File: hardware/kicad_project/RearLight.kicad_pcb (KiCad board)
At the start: 2 copper layers, 26 x 55.5 mm, 55 parts, among them J1 USB_C_Receptacle_USB2.0_16P, J2 Conn_02x03_Odd_Even, Q1 AO3400A, Q3 AO3400A, SW1 SW_Push, U1 453-00039R, U2 USBLC6-2SC6, U4 DW01A, U5 LIS3DH, U6 OPT3001DNPR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

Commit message: Layout 2nd draft
Todo: increase via size
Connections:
- U1 pad 33: GND -> unconnected-(U1-GND-Pad33)
- U1 pad 47: GND -> unconnected-(U1-GND-Pad47)
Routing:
- net GND: track 61.9 -> 92.6 mm, vias 46 -> 71
- net Net-(LED1-K): track 7.74 -> 0.00 mm
- net +VDD_nRF: track 121.4 -> 128.1 mm, vias 9 -> 10
- net Net-(LED1-A): track 4.80 -> 0.00 mm
- added copper zone on F.Cu, net Net-(LED1-A)
- added copper zone on F.Cu, net Net-(LED1-K)

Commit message: DFM design overhaul
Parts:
- removed H1, H2, H3, H4: M2, MountingHole:MountingHole_2.1mm
- removed LED2: LTRB_RASF.01-6B6C-C3E6-0-0-R18, RearLight:LTRBRASF016B6CC3E600R18
- removed R19: 100, Resistor_SMD:R_0402_1005Metric
- added D1: LED_R, LED_SMD:LED_0603_1608Metric, F.Cu at (150.5, 111.0)
- added D2: LED_Y, LED_SMD:LED_0805_2012Metric, F.Cu at (153.0, 110.8)
- added R16: 49R9, RearLight:R_0402_1005Metric_NO_SILK, F.Cu at (153.0, 113.6)
- C2, C3: footprint Capacitor_SMD:C_0603_1608Metric -> RearLight:C_0603_1608Metric_NO_SILK
- R1, R11, R5: footprint Resistor_SMD:R_0603_1608Metric -> RearLight:R_0603_1608Metric_NO_SILK
- R10, R12, R13, R14, R2, R3, R4, R6, R7, R8: footprint Resistor_SMD:R_0402_1005Metric -> RearLight:R_0402_1005Metric_NO_SILK
- U1: footprint Liard_BL653_ 453-00039_Custom:Laird_BL653 -> RF_Module:Laird_BL653
- moved R10 4.91 mm to (150.5, 113.6), turned to 90 degrees
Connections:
- U1 pad 22: RGB_B -> unconnected-(U1-SIO_14-Pad22)
- U1 pad 27: RGB_R -> RGB_Y
- U1 pad 28: RGB_G -> RGB_R
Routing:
- net RGB_B: track 14.3 -> 0.00 mm, vias 2 -> 0
- net RGB_G: track 10.8 -> 0.00 mm, vias 2 -> 0
- net RGB_Y: track 0.00 -> 9.81 mm
- net +VDD_nRF: track 128.1 -> 119.5 mm
- net Net-(LED2-A_RED): track 5.90 -> 0.00 mm
- net Net-(D1-A): track 6.60 -> 1.30 mm
- net Net-(D2-A): track 0.00 -> 1.34 mm
- net GND: track 92.6 -> 93.5 mm, vias 71 -> 72
- net RGB_R: track 9.46 -> 9.87 mm, vias 0 -> 2

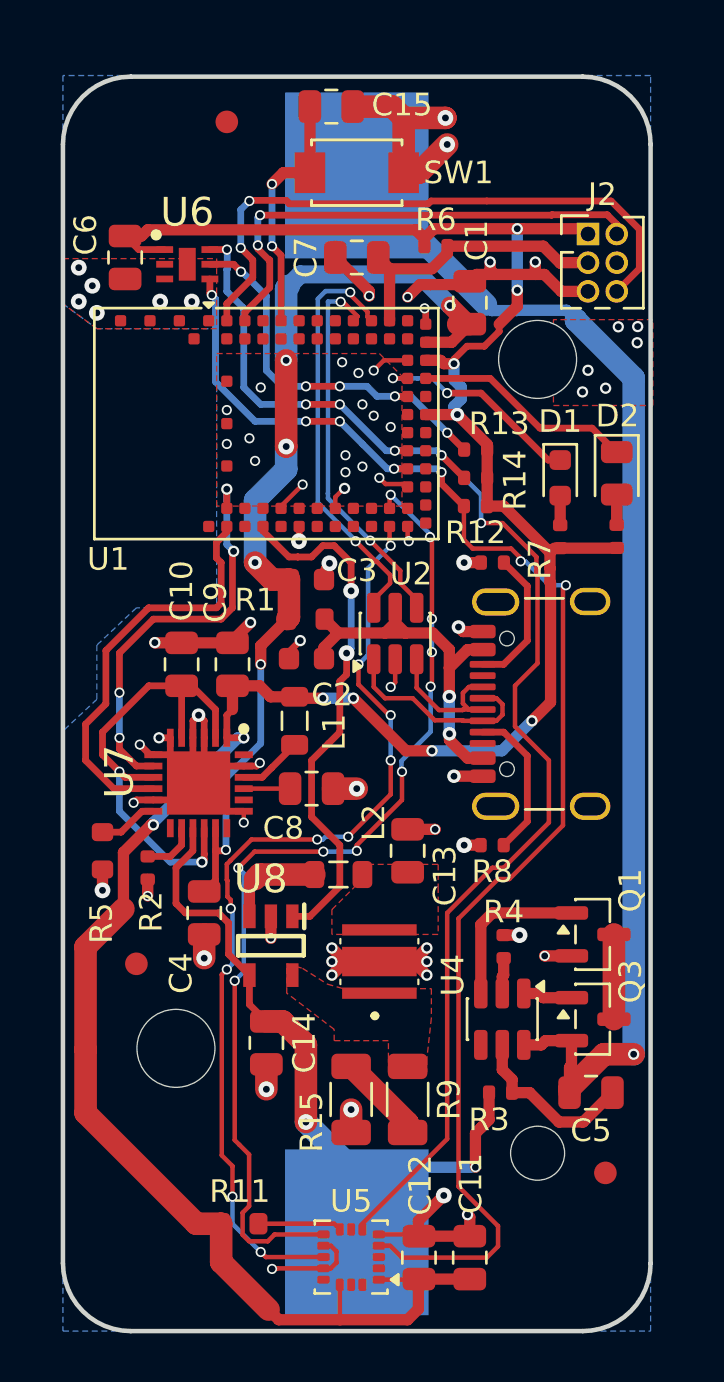
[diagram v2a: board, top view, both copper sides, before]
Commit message: Added correct tooling holes for JLCPCB assembly
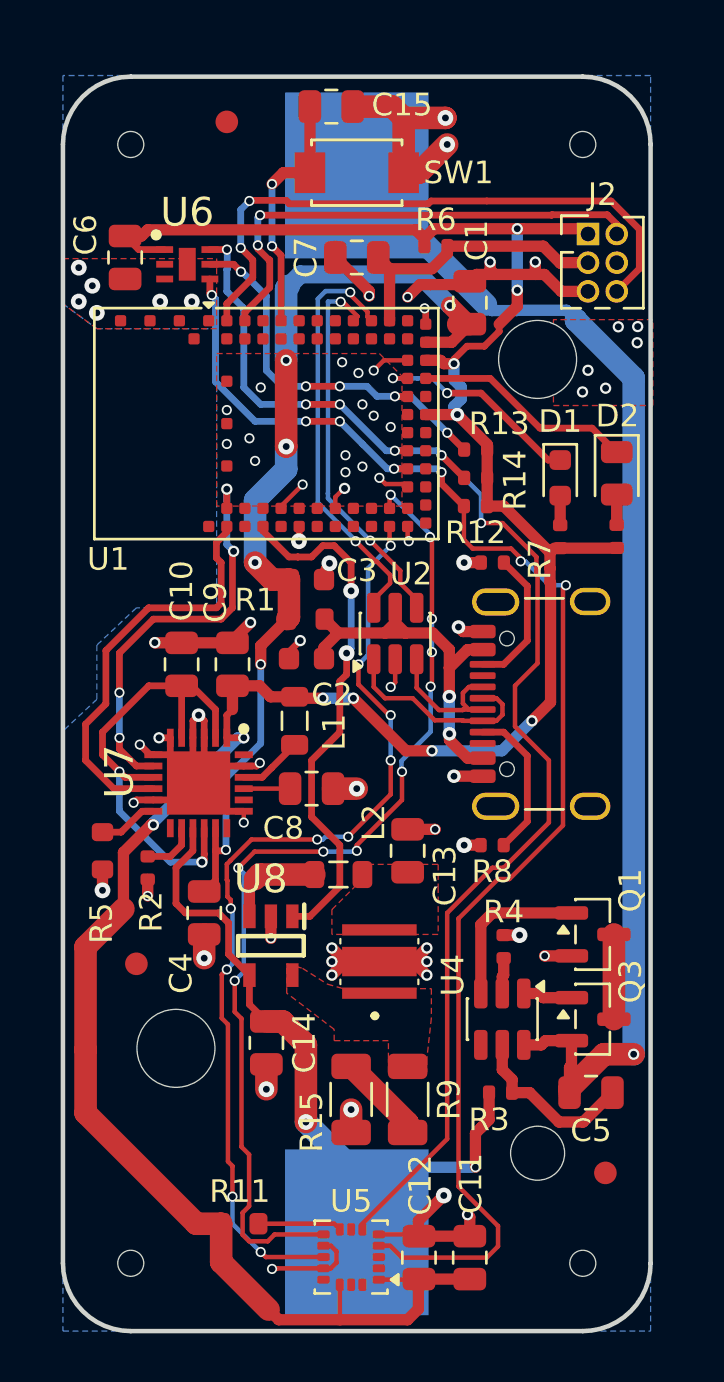
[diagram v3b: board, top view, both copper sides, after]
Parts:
- added H1: JLCPCB Tooling Hole, MountingHole:ToolingHole_1.152mm, F.Cu at (131.5, 96.2)
- added H2: JLCPCB Tooling Hole, MountingHole:ToolingHole_1.152mm, F.Cu at (151.5, 96.2)
- added H3: JLCPCB Tooling Hole, MountingHole:ToolingHole_1.152mm, F.Cu at (151.5, 145.8)
- added H4: JLCPCB Tooling Hole, MountingHole:ToolingHole_1.152mm, F.Cu at (131.5, 145.8)

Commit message: better placement & silkscreen for DFM
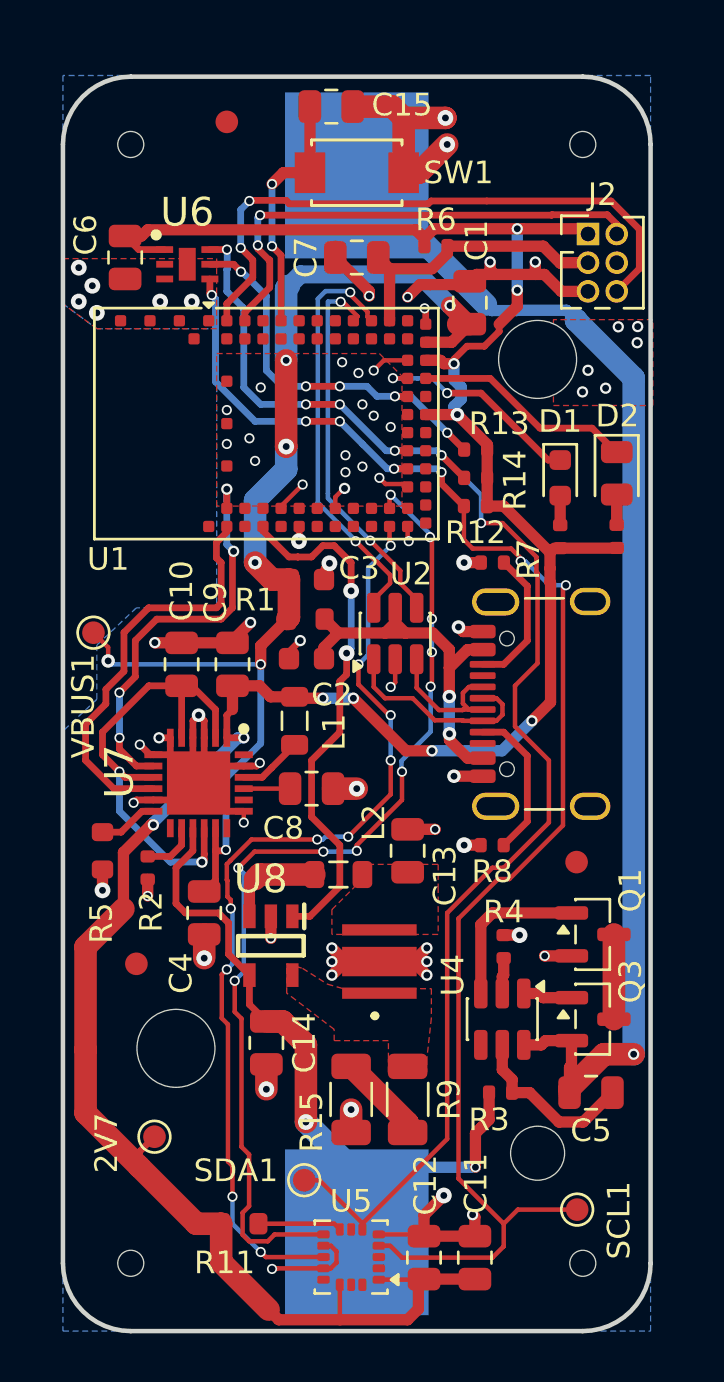
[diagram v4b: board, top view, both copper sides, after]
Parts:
- added 2V7: TestPoint, TestPoint:TestPoint_Pad_D1.0mm, F.Cu at (132.6, 140.2)
- added SCL1: TestPoint, TestPoint:TestPoint_Pad_D1.0mm, F.Cu at (151.2, 143.4)
- added SDA1: TestPoint, TestPoint:TestPoint_Pad_D1.0mm, F.Cu at (139.2, 142.1)
- added VBUS1: TestPoint, TestPoint:TestPoint_Pad_D1.0mm, F.Cu at (129.8, 117.8)
- moved FID1 13.8 mm to (151.2, 128.0)
- moved C11 0.22 mm to (146.7, 145.5)
- moved C12 0.22 mm to (144.5, 145.5)
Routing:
- net +VBUS_FIL: track 43.2 -> 51.5 mm, vias 6 -> 7
- net /I2C_SCL: track 63.7 -> 67.5 mm
- net /I2C_SDA: track 60.6 -> 64.2 mm
- net +VDD_nRF: track 119.5 -> 121.4 mm

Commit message: Added 100k pulldown to LED driver EN
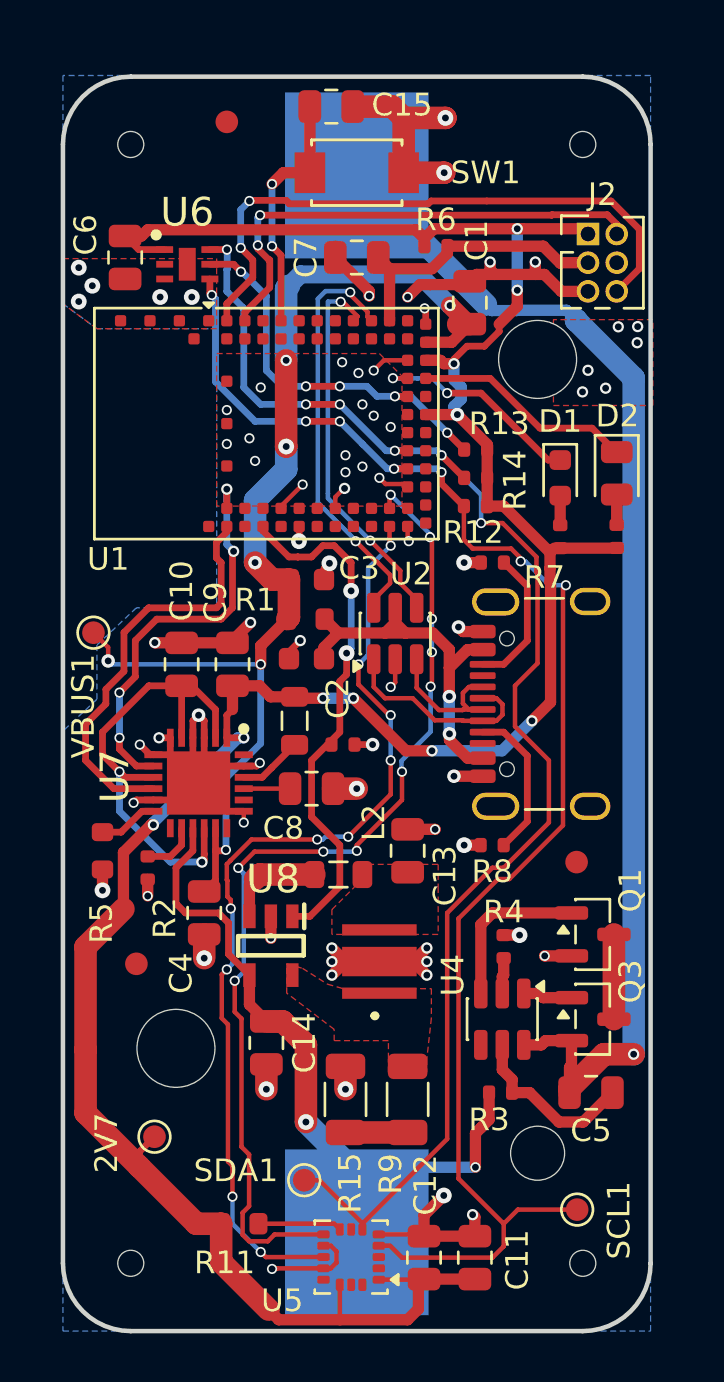
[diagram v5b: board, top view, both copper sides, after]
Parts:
- added R17: 100k, RearLight:R_0402_1005Metric_NO_SILK, F.Cu at (140.9, 122.8)
- U5: value LIS3DH -> LIS3DHTR
- moved R15 0.25 mm to (141.0, 138.5), turned to 90 degrees
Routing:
- net Net-(R15-Pad1): track 3.96 -> 2.75 mm

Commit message: Production Version 1.0
Moved red LED to NPM1100
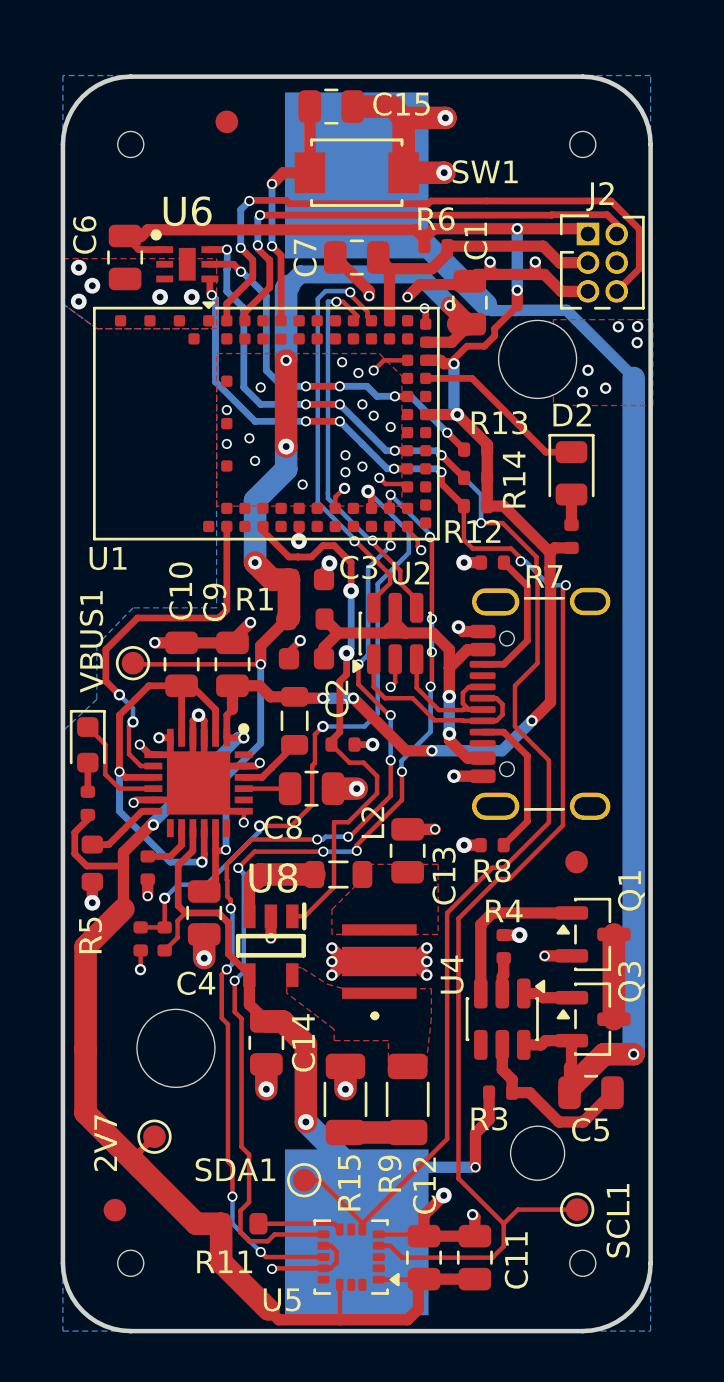
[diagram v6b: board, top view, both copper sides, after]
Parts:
- added R18: 1M, RearLight:R_0402_1005Metric_NO_SILK, F.Cu at (133.0, 131.4)
- added R19: 100k, RearLight:R_0402_1005Metric_NO_SILK, F.Cu at (131.9, 131.4)
- moved D1 24.0 mm to (129.6, 122.8)
- moved R10 24.0 mm to (129.6, 125.4), turned to -90 degrees
- moved FID3 10.9 mm to (130.8, 143.4)
- moved VBUS1 2.21 mm to (131.6, 119.2)
- moved D2 2.00 mm to (151.0, 110.8)
- moved R16 2.00 mm to (151.0, 113.6), turned to -90 degrees
- moved R5 0.71 mm to (129.8, 128.1)
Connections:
- D1 pad 1: RGB_R -> Net-(D1-K)
- R10 pad 1: +VDD_nRF -> Net-(D1-A)
- R10 pad 2: Net-(D1-A) -> +VDD_nRF
- R16 pad 1: +VDD_nRF -> Net-(D2-A)
- R16 pad 2: Net-(D2-A) -> +VDD_nRF
- U1 pad 28: RGB_R -> unconnected-(U1-SIO_12-Pad28)
- U1 pad 48: unconnected-(U1-SIO_29/AIN5-Pad48) -> Net-(U1-SIO_29/AIN5)
- U1 pad 63: ERR_SIG -> CHG_SIG
- U1 pad 64: CHG_SIG -> unconnected-(U1-SIO_39-Pad64)
- U7 pad 10: ERR_SIG -> Net-(D1-K)
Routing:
- net Net-(U1-SIO_29/AIN5): track 0.00 -> 29.0 mm, vias 0 -> 4
- net ERR_SIG: track 18.4 -> 0.00 mm
- net RGB_R: track 9.87 -> 0.00 mm, vias 2 -> 0
- net Net-(D1-K): track 0.00 -> 4.80 mm
- net +VBUS_FIL: track 51.5 -> 48.9 mm, vias 7 -> 6
- net +VDD_nRF: track 121.4 -> 123.8 mm
- net RGB_Y: track 9.81 -> 7.80 mm
- net +BATT: track 32.8 -> 34.7 mm
- net CHG_SIG: track 18.0 -> 16.3 mm, vias 4 -> 2
- net Net-(U1-NFC1/SIO_09): track 23.4 -> 24.5 mm
- net Net-(U7-ICHG): track 2.63 -> 3.31 mm
- net +VSYS: track 21.4 -> 20.8 mm
- net GND: track 93.6 -> 93.7 mm, vias 72 -> 73

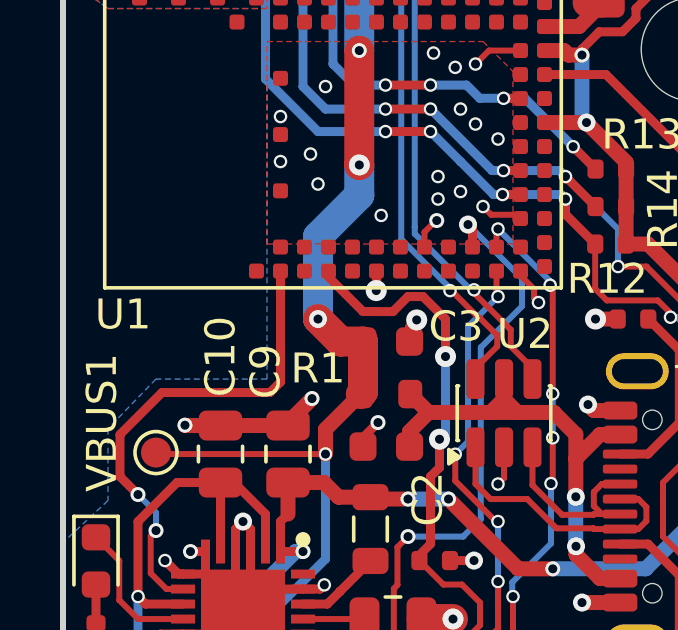
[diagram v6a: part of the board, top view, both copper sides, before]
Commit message: updated board thickness to 1.6 mm
The board was manufactured with 1.6 mm board thickness accidentaly.
To reflect this, updated the kicad project as well.
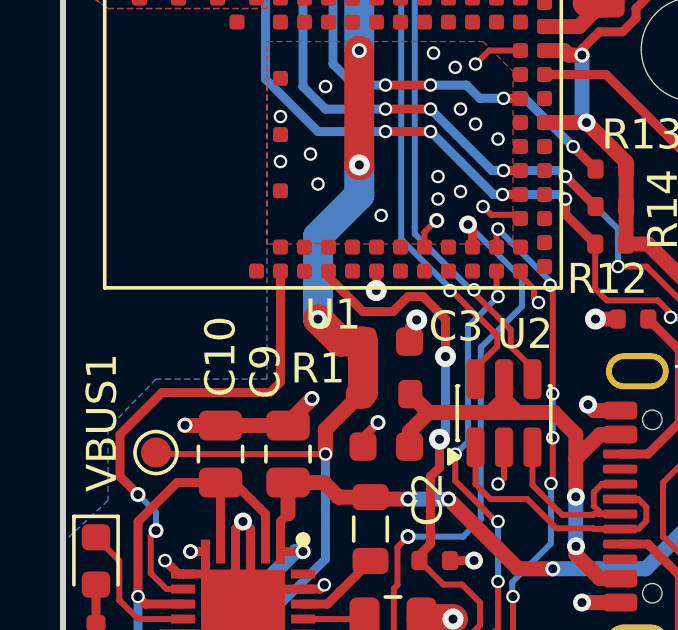
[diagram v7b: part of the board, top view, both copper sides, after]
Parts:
- U1: footprint RF_Module:Laird_BL653 -> Liard_BL653_ 453-00039_Custom:Laird_BL653
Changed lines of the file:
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@@
 	(generator_version "9.0")
 	(general
-		(thickness 0.9154)
+		(thickness 1.6)
 		(legacy_teardrops no)
 	)
@@
 			(layer "F.Mask"
 				(type "Top Solder Mask")
-				(thickness 0.01)
+				(thickness 0.0325)
 			)
 			(layer "F.Cu"
 				(type "copper")
-				(thickness 0.0152)
+				(thickness 0.035)
 			)
 			(layer "dielectric 1"
 				(type "core")
-				(thickness 0.865)
+				(thickness 1.465)
 				(material "FR4")
 				(epsilon_r 4.5)
@@
 			(layer "B.Cu"
 				(type "copper")
-				(thickness 0.0152)
+				(thickness 0.035)
 			)
 			(layer "B.Mask"
 				(type "Bottom Solder Mask")
-				(thickness 0.01)
+				(thickness 0.0325)
 			)
 			(layer "B.Paste"
@@
 		)
 	)
-	(footprint "RF_Module:Laird_BL653"
+	(footprint "Liard_BL653_ 453-00039_Custom:Laird_BL653"
 		(layer "F.Cu")
 		(at 137.5 108.6)
@@
 		(tags "Wi-Fi Module")
 		(property "Reference" "U1"
-			(at -7 6 180)
+			(at 0 6 180)
 			(layer "F.SilkS")
 			(effects
@@
 		)
 		(embedded_fonts no)
-		(model "${KICAD9_3DMODEL_DIR}/RF_Module.3dshapes/Laird_BL653.step"
+		(model "${KIPRJMOD}/../kicad_3d_models/BL653 453-00039_3D Model with label.STEP"
 			(offset
 				(xyz 0 0 0)
@@
 			)
 			(rotate
-				(xyz 0 0 0)
+				(xyz -90 -0 -90)
 			)
 		)
